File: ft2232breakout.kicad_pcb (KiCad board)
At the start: 2 copper layers, 43.2 x 35.6 mm, 24 parts, among them J1 USB_B_Micro, J2 Conn_01x20, J3 Conn_01x20, U1 FT2232H, U2 NCP1117-3.3_SOT223, U3 93CxxA

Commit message: Nearly there
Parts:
- added C15: 27pF, Capacitor_SMD:C_0603_1608Metric_Pad1.05x0.95mm_HandSolder, F.Cu at (163.0, 95.9)
- added C16: 27pF, Capacitor_SMD:C_0603_1608Metric_Pad1.05x0.95mm_HandSolder, F.Cu at (163.0, 99.1)
- added C17: 4.7uF, Capacitor_SMD:C_0603_1608Metric_Pad1.05x0.95mm_HandSolder, F.Cu at (157.5, 91.4)
- added R1: 12k, Resistor_SMD:R_0603_1608Metric_Pad1.05x0.95mm_HandSolder, F.Cu at (163.0, 102.0)
- added R2: 1k, Resistor_SMD:R_0603_1608Metric_Pad1.05x0.95mm_HandSolder, F.Cu at (171.4, 109.2)
- added R3: 2.2k, Resistor_SMD:R_0603_1608Metric_Pad1.05x0.95mm_HandSolder, F.Cu at (156.8, 109.9)
- added R4: 10k, Resistor_SMD:R_0603_1608Metric_Pad1.05x0.95mm_HandSolder, F.Cu at (158.1, 113.0)
- added R5: 10k, Resistor_SMD:R_0603_1608Metric_Pad1.05x0.95mm_HandSolder, F.Cu at (162.6, 113.0)
- added R6: 10k, Resistor_SMD:R_0603_1608Metric_Pad1.05x0.95mm_HandSolder, F.Cu at (162.6, 106.7)
- added Y1: 12MHz, Crystal:Crystal_SMD_3225-4Pin_3.2x2.5mm_HandSoldering, F.Cu at (168.0, 97.5)
- U3: value 93CxxA -> 93LCxxAxxOT; footprint Package_SO:SOIC-8_3.9x4.9mm_P1.27mm -> Package_TO_SOT_SMD:SOT-23-6
- moved C10 18.1 mm to (189.9, 106.7), turned to 270 degrees
- moved C12 16.2 mm to (174.1, 97.1), turned to 180 degrees
- moved C11 7.61 mm to (184.8, 112.4)
- moved C9 7.26 mm to (179.0, 112.4)
- moved C8 7.07 mm to (167.6, 109.2)
- moved C7 6.84 mm to (167.6, 106.0)
- moved C14 6.56 mm to (179.7, 95.0)
- moved C2 6.42 mm to (157.5, 101.6)
- moved C4 6.13 mm to (167.6, 102.9)
- moved U2 6.10 mm to (154.9, 96.5)
- moved C1 6.09 mm to (152.4, 101.6), turned to 180 degrees
- moved C5 6.06 mm to (186.1, 95.0)
- moved C13 4.89 mm to (189.9, 101.0), turned to 90 degrees
- moved C6 3.98 mm to (171.4, 106.0)
- moved J1 3.81 mm to (152.4, 108.0)
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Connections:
- net Net-(J2-Pad10) renamed /AD7
- net Net-(J2-Pad11) renamed /AC0
- net Net-(J2-Pad12) renamed /AC1
- net Net-(J2-Pad13) renamed /AC2
- net Net-(J2-Pad14) renamed /AC3
- net Net-(J2-Pad15) renamed /AC4
- net Net-(J2-Pad16) renamed /AC5
- net Net-(J2-Pad17) renamed /AC6
- net Net-(J2-Pad18) renamed /AC7
- net Net-(J2-Pad3) renamed /AD0
- net Net-(J2-Pad4) renamed /AD1
- net Net-(J2-Pad5) renamed /AD2
- net Net-(J2-Pad6) renamed /AD3
- net Net-(J2-Pad7) renamed /AD4
- net Net-(J2-Pad8) renamed /AD5
- net Net-(J2-Pad9) renamed /AD6
- net Net-(J3-Pad10) renamed /BD7
- net Net-(J3-Pad11) renamed /BC0
- net Net-(J3-Pad12) renamed /BC1
- net Net-(J3-Pad13) renamed /BC2
- net Net-(J3-Pad14) renamed /BC3
- net Net-(J3-Pad15) renamed /BC4
- net Net-(J3-Pad16) renamed /BC5
- net Net-(J3-Pad17) renamed /BC6
- net Net-(J3-Pad18) renamed /BC7
- net Net-(J3-Pad3) renamed /BD0
- net Net-(J3-Pad4) renamed /BD1
- net Net-(J3-Pad5) renamed /BD2
- net Net-(J3-Pad6) renamed /BD3
- net Net-(J3-Pad7) renamed /BD4
- net Net-(J3-Pad8) renamed /BD5
- net Net-(J3-Pad9) renamed /BD6
- J2 pad 1: Net-(J2-Pad1) -> +3V3
- J2 pad 19: Net-(J2-Pad19) -> /~SUSPEND
- J2 pad 2: Net-(J2-Pad2) -> GND
- J2 pad 20: Net-(J2-Pad20) -> GND
- J3 pad 1: Net-(J3-Pad1) -> +3V3
- J3 pad 19: Net-(J3-Pad19) -> /~PWREN
- J3 pad 2: Net-(J3-Pad2) -> GND
- J3 pad 20: Net-(J3-Pad20) -> GND
- U1 pad 1: Net-(U1-Pad1) -> GND
- U1 pad 10: Net-(U1-Pad10) -> GND
- U1 pad 11: Net-(U1-Pad11) -> GND
- U1 pad 13: Net-(U1-Pad13) -> GND
- U1 pad 15: Net-(U1-Pad15) -> GND
- U1 pad 25: Net-(U1-Pad25) -> GND
- U1 pad 35: Net-(U1-Pad35) -> GND
- U1 pad 36: Net-(U1-Pad36) -> /~SUSPEND
- U1 pad 47: Net-(U1-Pad47) -> GND
- U1 pad 5: Net-(U1-Pad5) -> GND
- U1 pad 51: Net-(U1-Pad51) -> GND
- U1 pad 60: Net-(U1-Pad60) -> /~PWREN
- U1 pad 61: Net-(U1-Pad61) -> Net-(R3-Pad2)
- U1 pad 62: Net-(U1-Pad62) -> Net-(R5-Pad1)
- U1 pad 63: Net-(U1-Pad63) -> Net-(R6-Pad1)
- U3 pad 2: Net-(U3-Pad2) -> GND
- U3 pad 3: Net-(U3-Pad3) -> Net-(R3-Pad2)
- U3 pad 4: Net-(U3-Pad4) -> Net-(R5-Pad1)
- U3 pad 5: Net-(U3-Pad5) -> Net-(R6-Pad1)
- U3 pad 6: Net-(U3-Pad6) -> +3V3
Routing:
- net +3V3: track 6.30 -> 69.2 mm, vias 4 -> 15
- net GND: track 0.00 -> 47.6 mm, vias 0 -> 10
- net +1V8: track 0.00 -> 45.6 mm
- net Net-(R3-Pad2): track 0.00 -> 33.2 mm, vias 0 -> 2
- net Net-(R6-Pad1): track 0.00 -> 27.6 mm, vias 0 -> 2
- net /BD2: track 0.00 -> 26.3 mm
- net /BD0: track 0.00 -> 25.6 mm
- net Net-(R5-Pad1): track 0.00 -> 25.2 mm, vias 0 -> 2
- net /BD6: track 0.00 -> 24.6 mm
- net /BD4: track 0.00 -> 24.0 mm
- net /BD3: track 0.00 -> 23.3 mm
- net Net-(J1-Pad3): track 0.00 -> 23.2 mm
- net Net-(J1-Pad2): track 0.00 -> 23.1 mm
- net /BC0: track 0.00 -> 22.7 mm
- net /~PWREN: track 0.00 -> 22.7 mm
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- added copper zone on F.Cu, net +3V3
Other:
- outline, holes or cut-outs redrawn
- net class Default: via_dia 0.8 -> 0.635; via_drill 0.4 -> 0.3
- rule pad_to_mask_clearance: 0.051 -> 0.0508
- board text added: "+3V3 GND"
- board text added: "AC0 AC1"
- board text added: "AC2 AC3"
- board text added: "AC4 AC5"
- board text added: "AC6 AC7"
- board text added: "AD0 AD1"
- board text added: "AD2 AD3"
- board text added: "AD4 AD5"
- board text added: "AD6 AD7"
- board text added: "BC1 BC0"
- board text added: "BC3 BC2"
- board text added: "BC5 BC4"
- board text added: "BC7 BC6"
- board text added: "BD1 BD0"
- board text added: "BD3 BD2"
- board text added: "BD5 BD4"
- board text added: "BD7 BD6"
- board text added: "FT2232H Breakout - rev. 1"
- board text added: "GND +3V3"
- board text added: "GND ~PWREN~"
- board text added: "~SUSPEND~ GND"

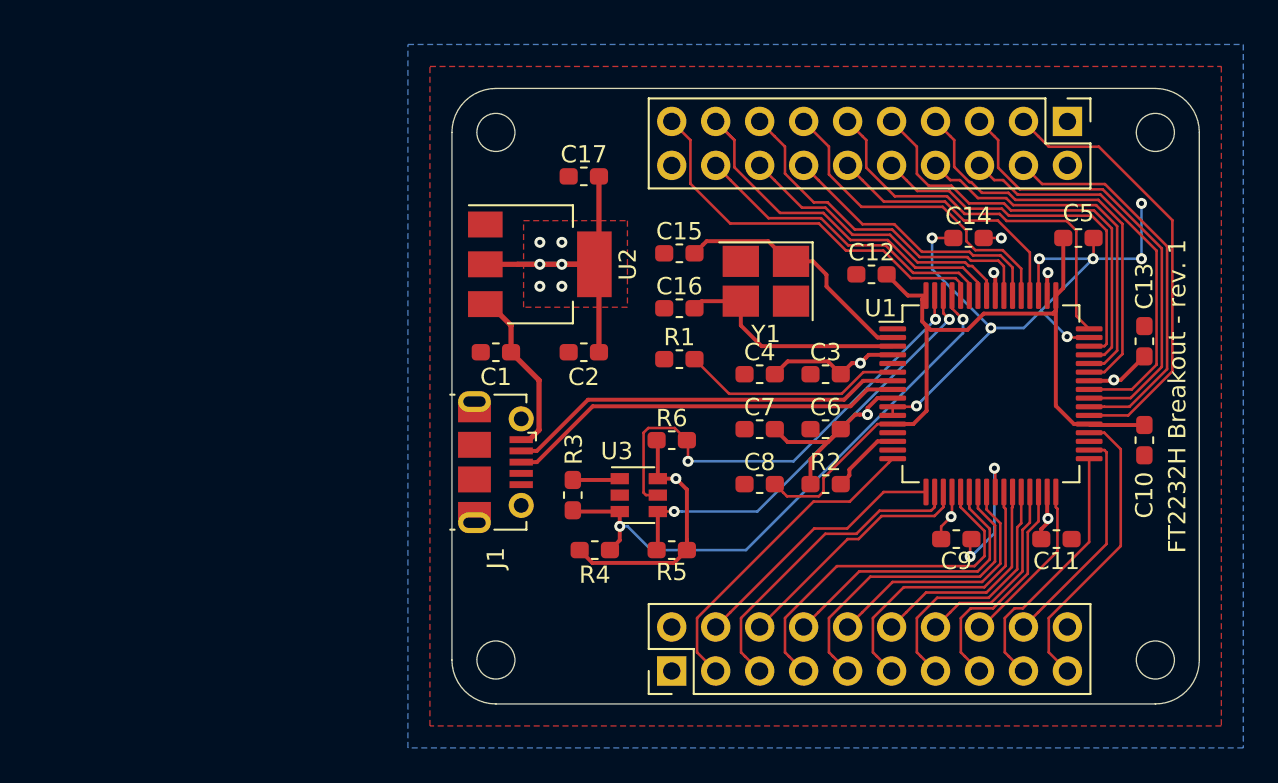
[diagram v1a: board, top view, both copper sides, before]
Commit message: Made board smaller
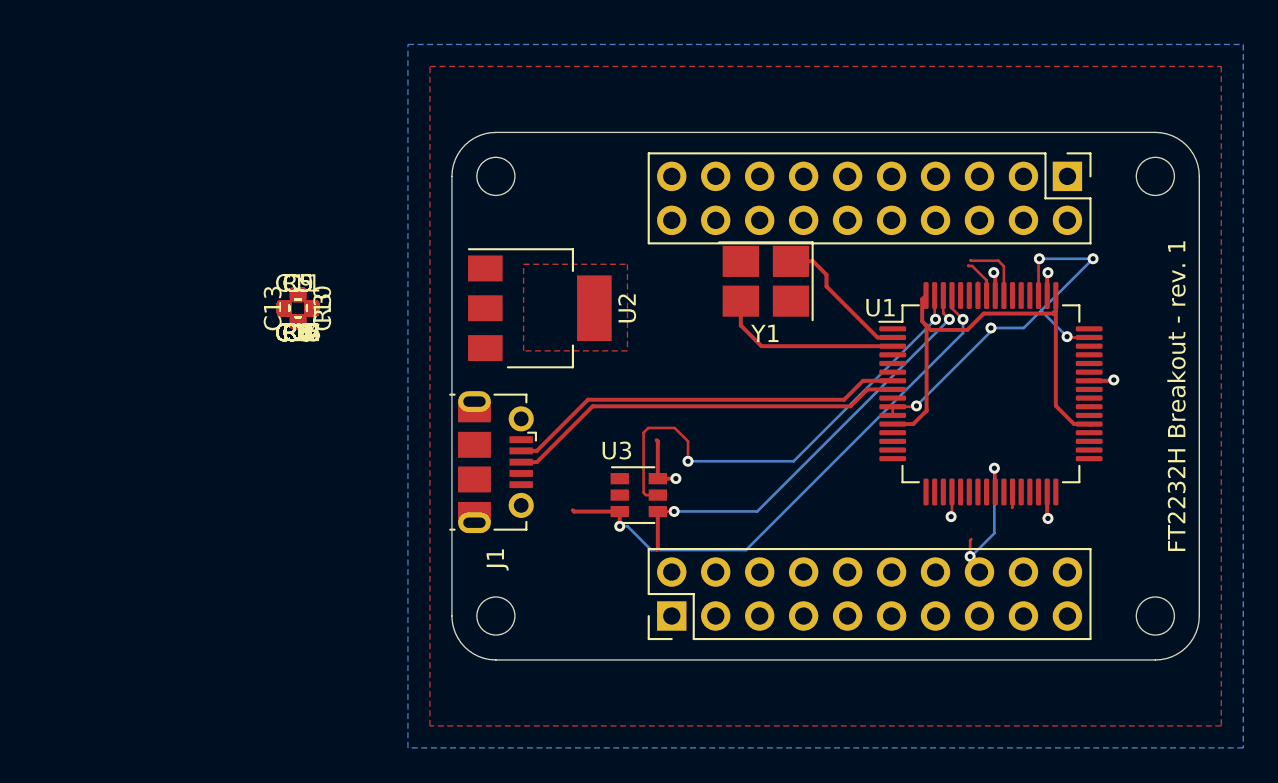
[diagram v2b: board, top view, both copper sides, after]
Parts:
- C1, C10, C11, C12, C13, C14, C15, C16, C17, C2, C3, C4, C5, C6, C7, C8, C9: footprint Capacitor_SMD:C_0603_1608Metric_Pad1.05x0.95mm_HandSolder -> Capacitor_SMD:C_0603_1608Metric
- R1, R2, R3, R4, R5, R6: footprint Resistor_SMD:R_0603_1608Metric_Pad1.05x0.95mm_HandSolder -> Resistor_SMD:R_0603_1608Metric
- U2: value NCP1117-3.3_SOT223 -> NCP1117ST33T3G
- moved C10 49.5 mm to (141.0, 99.1)
- moved C13 48.9 mm to (141.0, 99.1)
- moved C11 45.8 mm to (141.0, 99.1)
- moved C5 45.3 mm to (141.0, 99.1)
- moved C9 40.3 mm to (141.0, 99.1)
- moved C14 38.9 mm to (141.0, 99.1)
- moved C12 33.2 mm to (141.0, 99.1)
- moved R2 32.1 mm to (141.0, 99.1)
- moved C6 31.3 mm to (141.0, 99.1)
- moved C3 30.7 mm to (141.0, 99.1)
- moved C8 28.5 mm to (141.0, 99.1)
- moved C7 27.6 mm to (141.0, 99.1)
- moved C4 26.9 mm to (141.0, 99.1)
- moved R5 25.7 mm to (141.0, 99.1)
- moved R6 22.9 mm to (141.0, 99.1)
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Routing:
- net +3V3: track 69.2 -> 10.7 mm, vias 15 -> 6
- net /BD2: track 26.3 -> 0.00 mm
- net /BD0: track 25.6 -> 0.00 mm
- net /BD6: track 24.6 -> 0.00 mm
- net /BD4: track 24.0 -> 0.00 mm
- net /BD3: track 23.3 -> 0.00 mm
- net /BC0: track 22.7 -> 0.00 mm
- net /BD1: track 22.7 -> 0.00 mm
- net /~PWREN: track 22.7 -> 0.70 mm
- net /BD7: track 21.6 -> 0.00 mm
- net /BC6: track 22.2 -> 0.75 mm
- net /BD5: track 21.1 -> 0.00 mm
- net /AD4: track 20.8 -> 0.00 mm
- net /BC2: track 18.9 -> 0.00 mm
- net /AD6: track 18.9 -> 0.00 mm
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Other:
- board size 43.2 x 35.6 mm -> 43.2 x 30.5 mm

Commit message: Hmmm
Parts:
- removed the R5 at (141.0, 99.1)
- added R3: 10k, Resistor_SMD:R_0603_1608Metric, F.Cu at (166.9, 106.7)
- moved C5 48.3 mm to (189.2, 96.5)
- moved R5 31.9 mm to (171.9, 106.7)
- moved R4 30.9 mm to (171.4, 104.1)
- moved C7 30.5 mm to (171.4, 97.8)
- moved C8 30.5 mm to (171.4, 100.3)
- moved R6 27.9 mm to (166.4, 110.5)
- moved R1 21.1 mm to (158.8, 110.5)
- moved R2 19.3 mm to (158.8, 106.7)
- moved C3 18.9 mm to (158.8, 92.7), turned to 90 degrees
- moved C2 16.5 mm to (156.2, 92.7), turned to 90 degrees
- moved C17 15.7 mm to (137.2, 83.8)
- moved C15 14.2 mm to (143.5, 85.1)
- moved C6 14.0 mm to (127.0, 97.8)
- moved C1 13.7 mm to (153.7, 104.1)
- moved C14 12.7 mm to (133.3, 88.9)
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- renumbered C7 to C10, C8 to C11, C9 to C12, C10 to C13, C11 to C14, C12 to C15, C13 to C16, C14 to C17, C17 to C3, C15 to C4, C16 to C6, C3 to C7, C4 to C8, C6 to C9, R3 to R1, R4 to R2, R1 to R4, R2 to R5, U2 to U1, U3 to U2, U1 to U3
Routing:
- net GND: track 32.6 -> 0.00 mm, vias 7 -> 0
- net Net-(R1-Pad2): track 31.6 -> 0.00 mm, vias 2 -> 0
- net Net-(R6-Pad1): track 27.6 -> 0.00 mm, vias 2 -> 0
- net +1V8: track 26.9 -> 0.00 mm
- net Net-(R3-Pad1): track 25.2 -> 0.00 mm, vias 2 -> 0
- net Net-(J1-Pad3): track 23.2 -> 0.00 mm
- net Net-(J1-Pad2): track 23.1 -> 0.00 mm
- net /BD6: track 0.00 -> 21.6 mm, vias 0 -> 1
- net /BD2: track 0.00 -> 21.2 mm, vias 0 -> 1
- net /BD0: track 0.00 -> 21.2 mm, vias 0 -> 1
- net /BD4: track 0.00 -> 21.0 mm, vias 0 -> 1
- net /BD7: track 0.00 -> 19.5 mm, vias 0 -> 1
- net /BD3: track 0.00 -> 19.2 mm, vias 0 -> 1
- net /BD5: track 0.00 -> 19.0 mm, vias 0 -> 1
- net /BD1: track 0.00 -> 18.9 mm, vias 0 -> 1
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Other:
- net class Default: via_dia 0.635 -> 0.508; via_drill 0.3 -> 0.254
- rule via_min_drill: 0.3 -> 0.254
- rule via_min_size: 0.4 -> 0.508

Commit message: Hmmmm
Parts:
- moved C14 59.5 mm to (190.5, 105.4), turned to 90 degrees
- moved C17 59.1 mm to (189.2, 111.8)
- moved C16 51.7 mm to (190.5, 109.2)
- moved C13 48.7 mm to (189.2, 99.1), turned to 0 degrees
- moved C12 46.4 mm to (190.5, 101.6), turned to 90 degrees
- moved C11 43.9 mm to (171.9, 109.2)
- moved C6 36.9 mm to (163.8, 96.5)
- moved C10 35.8 mm to (172.7, 97.8), turned to 90 degrees
- moved C15 33.7 mm to (175.3, 96.5)
- moved C4 31.9 mm to (163.8, 104.1)
- moved C9 29.0 mm to (171.4, 97.8), turned to 90 degrees
- moved C8 2.84 mm to (170.2, 97.8), turned to 90 degrees
- moved C7 2.54 mm to (168.9, 97.8), turned to 90 degrees
